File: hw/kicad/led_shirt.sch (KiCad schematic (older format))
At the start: 20 parts, among them J1 10103593-0001LF, P6 b+, P7 b-, Q1 MOS_N_np, SW1 SW_PUSH, U1 MCP73831, U2 PIC12F1822

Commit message: save some changes. need to switch to dual n-fet package.
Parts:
- added Q1: MOSFET_N, symbol MOSFET_N
- C1, C2: symbol C -> C-RESCUE-led_shirt
- D1: renamed from D2; symbol LED -> LED-RESCUE-led_shirt
- D2: renamed from D3; symbol LED -> LED-RESCUE-led_shirt
- D3: renamed from D4; symbol LED -> LED-RESCUE-led_shirt
- D4: renamed from D5; symbol LED -> LED-RESCUE-led_shirt
- D5: renamed from D1; symbol LED -> LED-RESCUE-led_shirt
- R1: renamed from R3; symbol R -> R-RESCUE-led_shirt
- R2: renamed from R4; symbol R -> R-RESCUE-led_shirt
- R3: renamed from R5; symbol R -> R-RESCUE-led_shirt
- R4: renamed from R6; symbol R -> R-RESCUE-led_shirt
- R5: renamed from R2; symbol R -> R-RESCUE-led_shirt
- R6: renamed from R1; symbol R -> R-RESCUE-led_shirt
- renumbered P6 to P1, P7 to P2, Q1 to Q2, U2 to U1, U1 to U2
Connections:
- net GND: now also R1.2; no longer SW1.1
- net mclr: now also J1.3 (D+)
- net vbat: now also SW1.1, Q1.3 (D); no longer R1.1, U1.1 (VDD)
- net icspdat: now reaches J1.2 (D-)
- net icspdat: now also U1.7 (RA0)
- net icspclk: now reaches J1.4 (ID)
- net icspclk: now also U1.6 (RA1)
- net at SW1.2, U1.2 (RA5): now also R1.1, Q1.1 (G); no longer R1.2
- new net: Q1.2 (S), U1.1 (VDD)
- no-connect marks 7 -> 1
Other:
- note removed: "icspclk"
- note removed: "icspdat"
- moved on the sheet: R1, SW1
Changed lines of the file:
@@
 EESchema Schematic File Version 2
+LIBS:led_shirt-rescue
 LIBS:power
 LIBS:device
@@
 LIBS:memory
 LIBS:xilinx
-LIBS:special
 LIBS:microcontrollers
 LIBS:dsp
@@
 LIBS:extra
 LIBS:led_shirt-cache
-EELAYER 27 0
+EELAYER 25 0
 EELAYER END
 $Descr A4 11693 8268
@@
 vbat
 $Comp
-L MOS_N_np Q1
+L MOS_N_np Q2
 U 1 1 50A55C00
 P 8500 3650
-F 0 "Q1" H 8510 3820 60  0000 R CNN
+F 0 "Q2" H 8510 3820 60  0000 R CNN
 F 1 "MOS_N_np" H 8510 3500 60  0000 R CNN
 F 2 "" H 8500 3650 60  0001 C CNN
@@
 	1    0    0    -1
 $EndComp
-Text GLabel 5450 1900 0    60   Input ~ 0
+Text GLabel 4250 1800 0    60   Input ~ 0
 vbat
 $Comp
-L R R3
+L R-RESCUE-led_shirt R1
 U 1 1 509FF0CA
-P 5450 2300
-F 0 "R3" V 5530 2300 50  0000 C CNN
-F 1 "10kΩ" V 5450 2300 50  0000 C CNN
-F 2 "" H 5450 2300 60  0001 C CNN
-F 3 "" H 5450 2300 60  0001 C CNN
-	1    5450 2300
-	1    0    0    -1
-$EndComp
-$Comp
-L GND #PWR01
-U 1 1 509FF06B
-P 4650 2700
-F 0 "#PWR01" H 4650 2700 30  0001 C CNN
-F 1 "GND" H 4650 2630 30  0001 C CNN
-F 2 "" H 4650 2700 60  0001 C CNN
-F 3 "" H 4650 2700 60  0001 C CNN
-	1    4650 2700
-	1    0    0    -1
-$EndComp
-$Comp
-L SW_PUSH SW1
-U 1 1 509ED3DD
-P 5050 2650
-F 0 "SW1" H 5200 2760 50  0000 C CNN
-F 1 "SW_PUSH" H 5050 2570 50  0000 C CNN
-F 2 "" H 5050 2650 60  0001 C CNN
-F 3 "" H 5050 2650 60  0001 C CNN
-	1    5050 2650
-	1    0    0    -1
-$EndComp
-$Comp
-L R R4
+P 5050 3000
+F 0 "R1" V 5130 3000 50  0000 C CNN
+F 1 "10kΩ" V 5050 3000 50  0000 C CNN
+F 2 "" H 5050 3000 60  0001 C CNN
+F 3 "" H 5050 3000 60  0001 C CNN
+	1    5050 3000
+	1    0    0    -1
+$EndComp
+$Comp
+L R-RESCUE-led_shirt R2
 U 1 1 509E9C0F
 P 8600 3050
-F 0 "R4" V 8680 3050 50  0000 C CNN
+F 0 "R2" V 8680 3050 50  0000 C CNN
 F 1 "0Ω" V 8600 3050 50  0000 C CNN
 F 2 "" H 8600 3050 60  0001 C CNN
@@
 mclr
 $Comp
-L GND #PWR02
+L GND-RESCUE-led_shirt #PWR1
 U 1 1 509D14DE
 P 3250 1650
-F 0 "#PWR02" H 3250 1650 30  0001 C CNN
+F 0 "#PWR1" H 3250 1650 30  0001 C CNN
 F 1 "GND" H 3250 1580 30  0001 C CNN
 F 2 "" H 3250 1650 60  0001 C CNN
@@
 vbat
 $Comp
-L TST P7
+L TST P2
 U 1 1 509D14C3
 P 3250 1450
-F 0 "P7" H 3250 1750 40  0000 C CNN
+F 0 "P2" H 3250 1750 40  0000 C CNN
 F 1 "b-" H 3250 1700 30  0000 C CNN
 F 2 "" H 3250 1450 60  0001 C CNN
@@
 $EndComp
 $Comp
-L TST P6
+L TST P1
 U 1 1 509D14B5
 P 3100 1450
-F 0 "P6" H 3100 1750 40  0000 C CNN
+F 0 "P1" H 3100 1750 40  0000 C CNN
 F 1 "b+" H 3100 1700 30  0000 C CNN
 F 2 "" H 3100 1450 60  0001 C CNN
@@
 $EndComp
 $Comp
-L GND #PWR03
+L GND-RESCUE-led_shirt #PWR3
 U 1 1 509D02E2
 P 7450 2400
-F 0 "#PWR03" H 7450 2400 30  0001 C CNN
+F 0 "#PWR3" H 7450 2400 30  0001 C CNN
 F 1 "GND" H 7450 2330 30  0001 C CNN
 F 2 "" H 7450 2400 60  0001 C CNN
@@
 	1    0    0    -1
 $EndComp
-Text GLabel 5900 2500 0    60   Input ~ 0
+Text GLabel 5450 1500 2    60   Input ~ 0
 vbat
 Text GLabel 5350 5250 2    60   Input ~ 0
 vbat
 $Comp
-L GND #PWR04
+L GND-RESCUE-led_shirt #PWR7
 U 1 1 509D029F
 P 4900 6150
-F 0 "#PWR04" H 4900 6150 30  0001 C CNN
+F 0 "#PWR7" H 4900 6150 30  0001 C CNN
 F 1 "GND" H 4900 6080 30  0001 C CNN
 F 2 "" H 4900 6150 60  0001 C CNN
@@
 $EndComp
 $Comp
-L C C2
+L C-RESCUE-led_shirt C2
 U 1 1 509D0292
 P 5050 5550
@@
 $EndComp
 $Comp
-L R R2
+L R-RESCUE-led_shirt R5
 U 1 1 509D0279
 P 4650 5650
-F 0 "R2" V 4730 5650 50  0000 C CNN
+F 0 "R5" V 4730 5650 50  0000 C CNN
 F 1 "3.3kΩ" V 4650 5650 50  0000 C CNN
 F 2 "" H 4650 5650 60  0001 C CNN
@@
 $EndComp
 $Comp
-L R R1
+L R-RESCUE-led_shirt R6
 U 1 1 509D021A
 P 2900 6100
-F 0 "R1" V 2980 6100 50  0000 C CNN
+F 0 "R6" V 2980 6100 50  0000 C CNN
 F 1 "3.3kΩ" V 2900 6100 50  0000 C CNN
 F 2 "" H 2900 6100 60  0001 C CNN
@@
 $EndComp
 $Comp
-L LED D1
+L LED-RESCUE-led_shirt D5
 U 1 1 509D01E7
 P 2900 5550
-F 0 "D1" H 2900 5650 50  0000 C CNN
+F 0 "D5" H 2900 5650 50  0000 C CNN
 F 1 "LED" H 2900 5450 50  0000 C CNN
 F 2 "" H 2900 5550 60  0001 C CNN
@@
 $EndComp
 $Comp
-L C C1
+L C-RESCUE-led_shirt C1
 U 1 1 509D016A
 P 2450 5550
@@
 $EndComp
 $Comp
-L GND #PWR05
+L GND-RESCUE-led_shirt #PWR6
 U 1 1 509D017A
 P 2450 5850
-F 0 "#PWR05" H 2450 5850 30  0001 C CNN
+F 0 "#PWR6" H 2450 5850 30  0001 C CNN
 F 1 "GND" H 2450 5780 30  0001 C CNN
 F 2 "" H 2450 5850 60  0001 C CNN
@@
 vbus
 $Comp
-L GND #PWR06
+L GND-RESCUE-led_shirt #PWR2
 U 1 1 509D0101
 P 1800 1850
-F 0 "#PWR06" H 1800 1850 30  0001 C CNN
+F 0 "#PWR2" H 1800 1850 30  0001 C CNN
 F 1 "GND" H 1800 1780 30  0001 C CNN
 F 2 "" H 1800 1850 60  0001 C CNN
@@
 $EndComp
 $Comp
-L MCP73831 U1
+L MCP73831 U2
 U 1 1 508746F6
 P 3850 5400
-F 0 "U1" H 3850 5100 60  0000 C CNN
+F 0 "U2" H 3850 5100 60  0000 C CNN
 F 1 "MCP73831" H 3850 5700 60  0000 C CNN
 F 2 "" H 3850 5400 60  0001 C CNN
@@
 $EndComp
 $Comp
-L GND #PWR07
+L GND-RESCUE-led_shirt #PWR5
 U 1 1 52607FD1
 P 8150 4500
-F 0 "#PWR07" H 8150 4500 30  0001 C CNN
+F 0 "#PWR5" H 8150 4500 30  0001 C CNN
 F 1 "GND" H 8150 4430 30  0001 C CNN
 F 2 "" H 8150 4500 60  0000 C CNN
@@
 $EndComp
 $Comp
-L PIC12F1822 U2
+L PIC12F1822 U1
 U 1 1 52608131
 P 6600 2700
-F 0 "U2" H 6600 2250 60  0000 C CNN
+F 0 "U1" H 6600 2250 60  0000 C CNN
 F 1 "PIC12F1822" H 6600 3100 60  0000 C CNN
 F 2 "" H 6650 2650 60  0000 C CNN
@@
 $EndComp
 $Comp
-L R R5
+L R-RESCUE-led_shirt R3
 U 1 1 5267E075
 P 5950 3300
-F 0 "R5" V 6030 3300 40  0000 C CNN
+F 0 "R3" V 6030 3300 40  0000 C CNN
 F 1 "10K" V 5957 3301 40  0000 C CNN
 F 2 "~" V 5880 3300 30  0000 C CNN
@@
 vbat
 $Comp
-L R R6
+L R-RESCUE-led_shirt R4
 U 1 1 5267E19B
 P 7700 4000
-F 0 "R6" V 7780 4000 40  0000 C CNN
+F 0 "R4" V 7780 4000 40  0000 C CNN
 F 1 "10K" V 7707 4001 40  0000 C CNN
 F 2 "~" V 7630 4000 30  0000 C CNN
@@
 $EndComp
 $Comp
-L LED D2
+L LED-RESCUE-led_shirt D1
 U 1 1 52798086
 P 8600 2350
-F 0 "D2" H 8600 2450 50  0000 C CNN
+F 0 "D1" H 8600 2450 50  0000 C CNN
 F 1 "LED" H 8600 2250 50  0000 C CNN
 F 2 "" H 8600 2350 60  0001 C CNN
@@
 $EndComp
 $Comp
-L LED D3
+L LED-RESCUE-led_shirt D2
 U 1 1 5279808E
 P 8900 2350
-F 0 "D3" H 8900 2450 50  0000 C CNN
+F 0 "D2" H 8900 2450 50  0000 C CNN
 F 1 "LED" H 8900 2250 50  0000 C CNN
 F 2 "" H 8900 2350 60  0001 C CNN
@@
 $EndComp
 $Comp
-L LED D4
+L LED-RESCUE-led_shirt D3
 U 1 1 52798094
 P 9200 2350
-F 0 "D4" H 9200 2450 50  0000 C CNN
+F 0 "D3" H 9200 2450 50  0000 C CNN
 F 1 "LED" H 9200 2250 50  0000 C CNN
 F 2 "" H 9200 2350 60  0001 C CNN
@@
 $EndComp
 $Comp
-L LED D5
+L LED-RESCUE-led_shirt D4
 U 1 1 5279809A
 P 9500 2350
-F 0 "D5" H 9500 2450 50  0000 C CNN
+F 0 "D4" H 9500 2450 50  0000 C CNN
 F 1 "LED" H 9500 2250 50  0000 C CNN
 F 2 "" H 9500 2350 60  0001 C CNN
@@
 	0    1    1    0
 $EndComp
-NoConn ~ 1650 1350
-NoConn ~ 1650 1450
-NoConn ~ 1650 1550
-Text Notes 7300 2700 0    60   ~ 0
-icspdat
-NoConn ~ 7200 2650
-Text Notes 7300 2850 0    60   ~ 0
-icspclk
-NoConn ~ 7200 2800
-NoConn ~ 4600 2800
-Wire Wire Line
-	5450 1900 5450 2050
-Wire Wire Line
-	4750 2650 4650 2650
-Wire Wire Line
-	4650 2650 4650 2700
 Wire Wire Line
 	5900 2950 6000 2950
@@
 Connection ~ 4900 6000
 Wire Wire Line
-	5900 2500 6000 2500
+	5450 2500 6000 2500
 Wire Wire Line
 	3100 1450 3100 1600
@@
 Wire Wire Line
 	8600 2550 8600 2800
-Wire Wire Line
-	5350 2650 6000 2650
-Wire Wire Line
-	5450 2550 5450 2650
-Connection ~ 5450 2650
 Wire Wire Line
 	8300 3650 7200 3650
@@
 Connection ~ 8900 2550
 NoConn ~ 6000 2800
+$Comp
+L MOSFET_N Q1
+U 1 1 56337151
+P 5350 1800
+F 0 "Q1" H 5360 1970 60  0000 R CNN
+F 1 "MOSFET_N" H 5950 1800 60  0000 R CNN
+F 2 "" H 5350 1800 60  0000 C CNN
+F 3 "" H 5350 1800 60  0000 C CNN
+	1    5350 1800
+	1    0    0    -1
+$EndComp
+Wire Wire Line
+	5450 1500 5450 1600
+$Comp
+L SW_PUSH SW1
+U 1 1 509ED3DD
+P 4650 1800
+F 0 "SW1" H 4800 1910 50  0000 C CNN
+F 1 "SW_PUSH" H 4650 1720 50  0000 C CNN
+F 2 "" H 4650 1800 60  0001 C CNN
+F 3 "" H 4650 1800 60  0001 C CNN
+	1    4650 1800
+	1    0    0    -1
+$EndComp
+Wire Wire Line
+	4950 1800 5150 1800
+$Comp
+L GND-RESCUE-led_shirt #PWR4
+U 1 1 56338053
+P 5050 3350
+F 0 "#PWR4" H 5050 3350 30  0001 C CNN
+F 1 "GND" H 5050 3280 30  0001 C CNN
+F 2 "" H 5050 3350 60  0001 C CNN
+F 3 "" H 5050 3350 60  0001 C CNN
+	1    5050 3350
+	1    0    0    -1
+$EndComp
+Wire Wire Line
+	5050 1800 5050 2750
+Connection ~ 5050 1800
+Wire Wire Line
+	4350 1800 4250 1800
+Wire Wire Line
+	5050 3250 5050 3350
+Wire Wire Line
+	5450 2000 5450 2500
+Wire Wire Line
+	6000 2650 5050 2650
+Connection ~ 5050 2650
+Text GLabel 1800 1450 2    60   Input ~ 0
+mclr
+Text GLabel 7300 2650 2    60   Input ~ 0
+icspdat
+Text GLabel 7300 2800 2    60   Input ~ 0
+icspclk
+Wire Wire Line
+	7300 2650 7200 2650
+Wire Wire Line
+	7300 2800 7200 2800
+Text GLabel 2050 1350 2    60   Input ~ 0
+icspdat
+Text GLabel 2050 1550 2    60   Input ~ 0
+icspclk
+Wire Wire Line
+	2050 1350 1650 1350
+Wire Wire Line
+	1800 1450 1650 1450
+Wire Wire Line
+	1650 1550 2050 1550
 $EndSCHEMATC

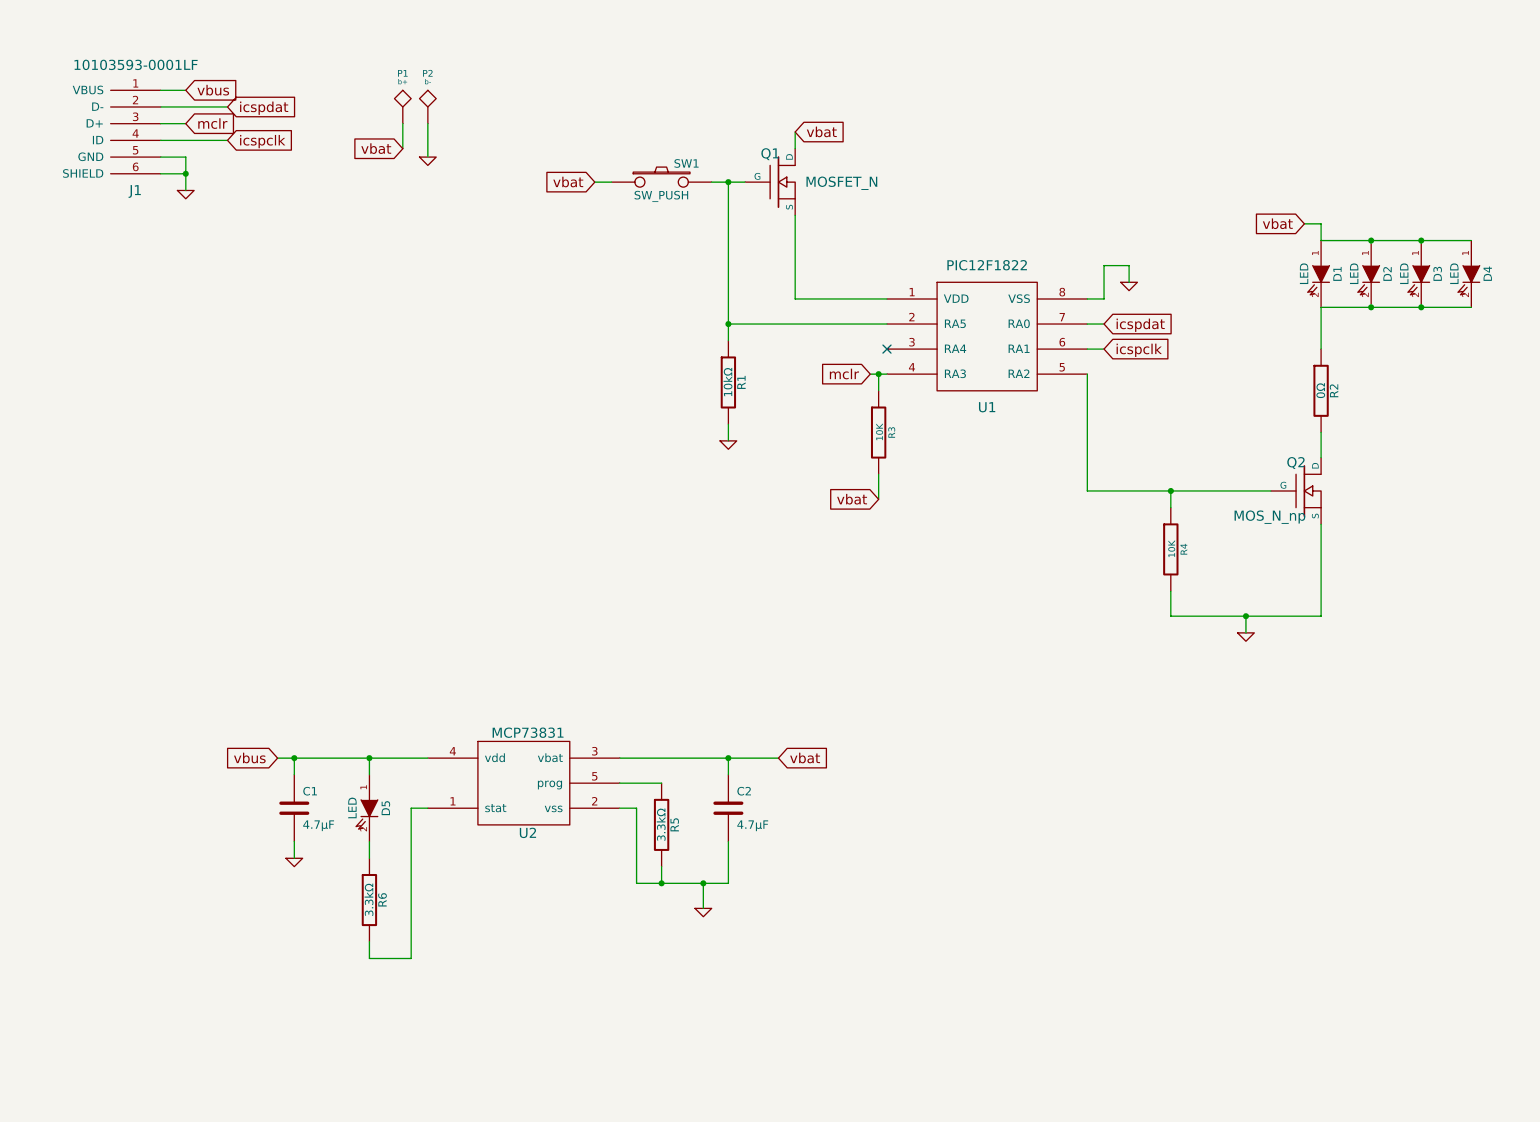
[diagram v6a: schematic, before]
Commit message: fix up fet symbol and connect it
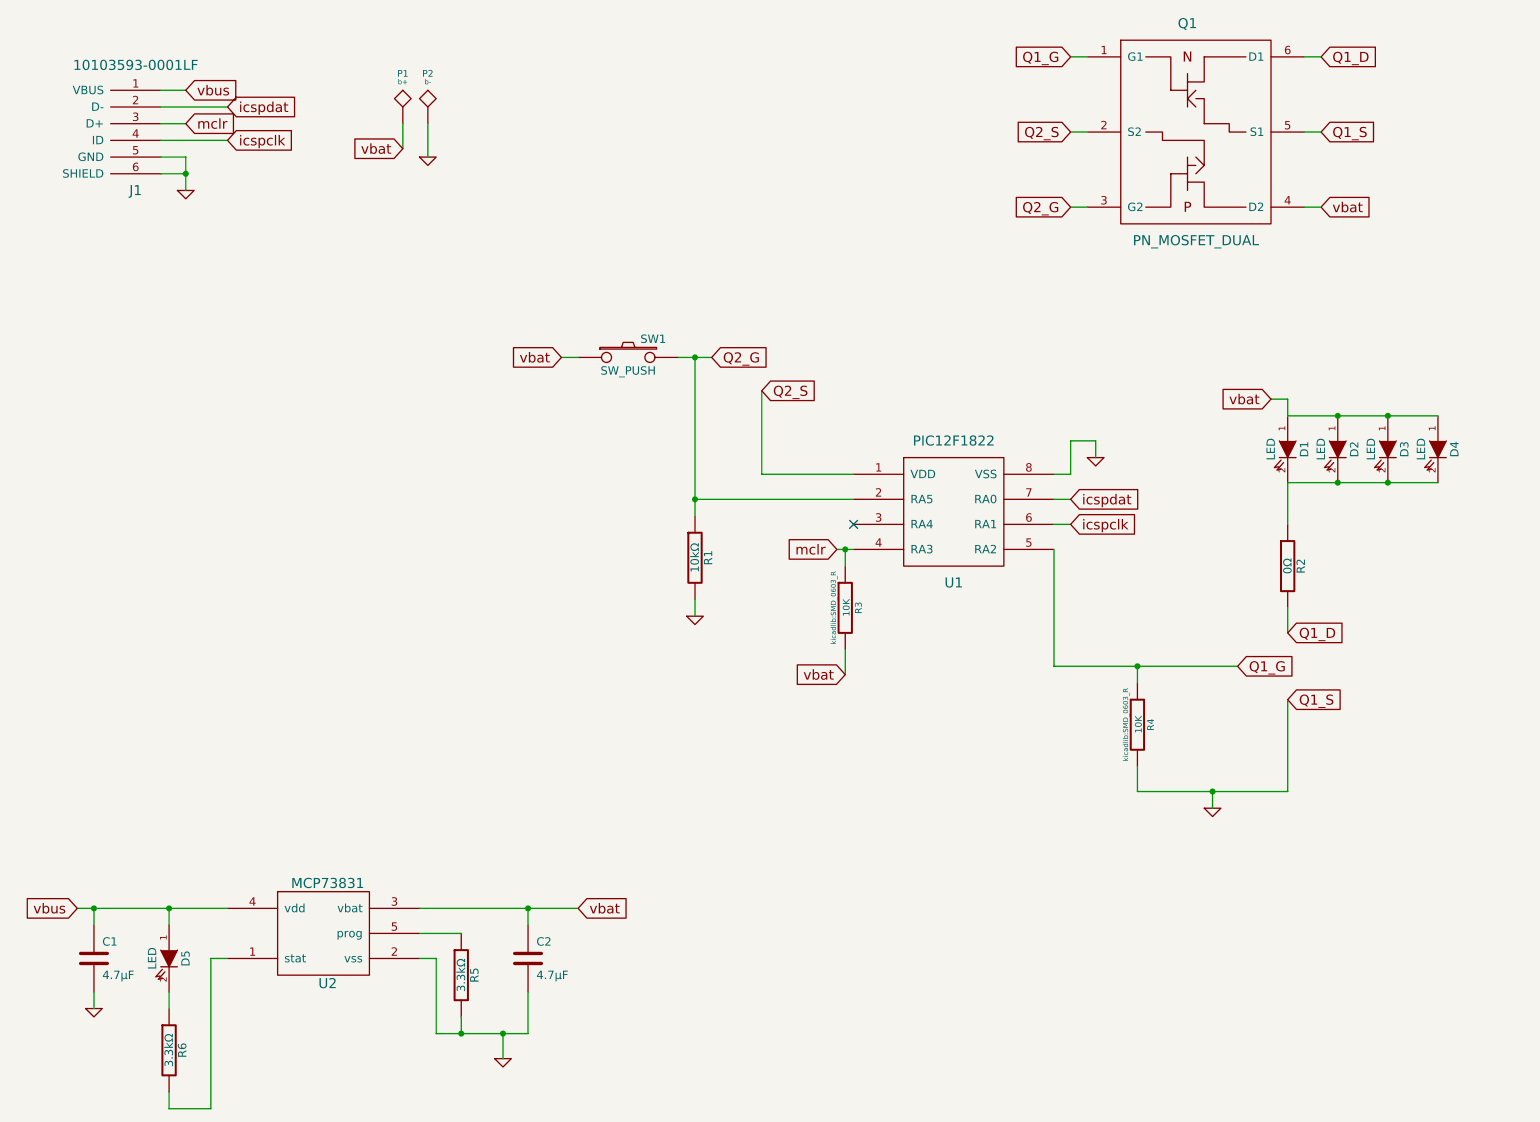
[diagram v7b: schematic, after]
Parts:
- removed Q1: MOSFET_N, symbol MOSFET_N
- removed Q2: MOS_N_np, symbol MOS_N_np
- added Q1: PN_MOSFET_DUAL, symbol PN_MOSFET_DUAL
- C1, C2, R1, R2, R5, R6: footprint (none) -> kicadlib:SMD_0603_R
- D1, D2, D3, D4, D5: footprint (none) -> kicadlib:plcc2
- J1: footprint (none) -> kicadlib:usb_micro_b_smt
- P1: footprint (none) -> noah:noah_hole_1
- P2: footprint (none) -> kicadlib:med_test_hole
- R3, R4: footprint ~ -> kicadlib:SMD_0603_R
- U1: footprint (none) -> noah:PIC12F1822-SOIC-8
- U2: footprint (none) -> kicadlib:MCP73831
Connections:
- net GND: now also Q1.5 (S1)
- net vbat: now also Q1.4 (D2)
- net Q1_D: now reaches R2.2
- net Q1_D: now also Q1.6 (D1)
- net Q2_G: now reaches R1.1, SW1.2, U1.2 (RA5)
- net Q2_G: now also Q1.3 (G2)
- net Q1_G: now reaches R4.1, U1.5 (RA2)
- net Q1_G: now also Q1.1 (G1)
- net Q2_S: now reaches U1.1 (VDD)
- net Q2_S: now also Q1.2 (S2)
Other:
- moved on the sheet: C1, C2, D1, D2, D3, D4, D5, R1, R2, R3, R4, R5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
